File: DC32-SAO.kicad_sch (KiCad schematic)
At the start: 11 parts, among them J1 Conn_01x06_Male

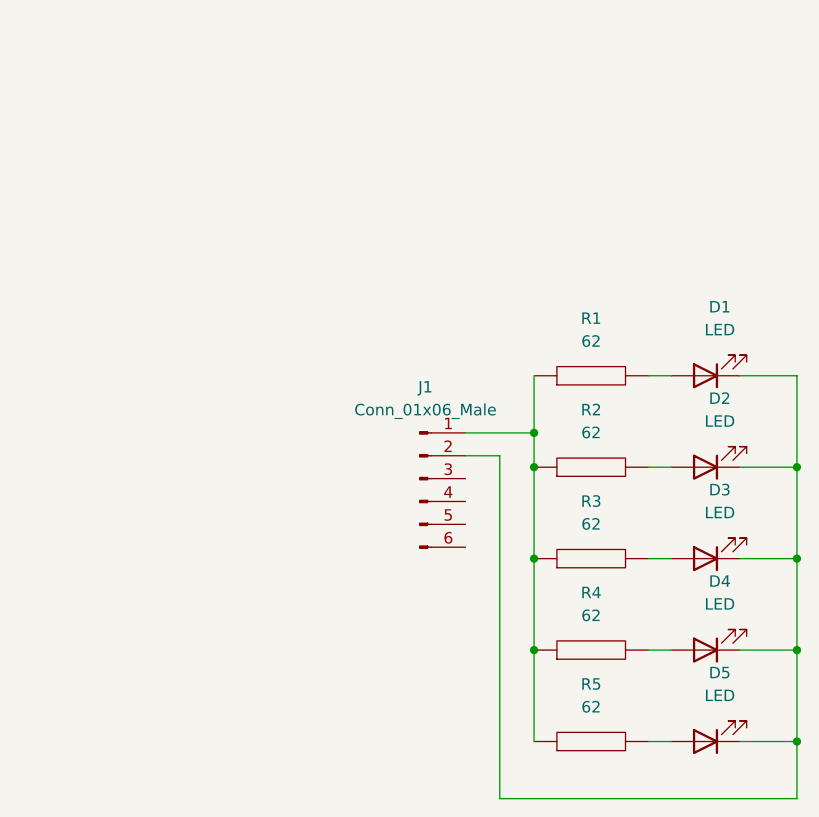
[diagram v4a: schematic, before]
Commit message: Changed Resistors to through-hole.
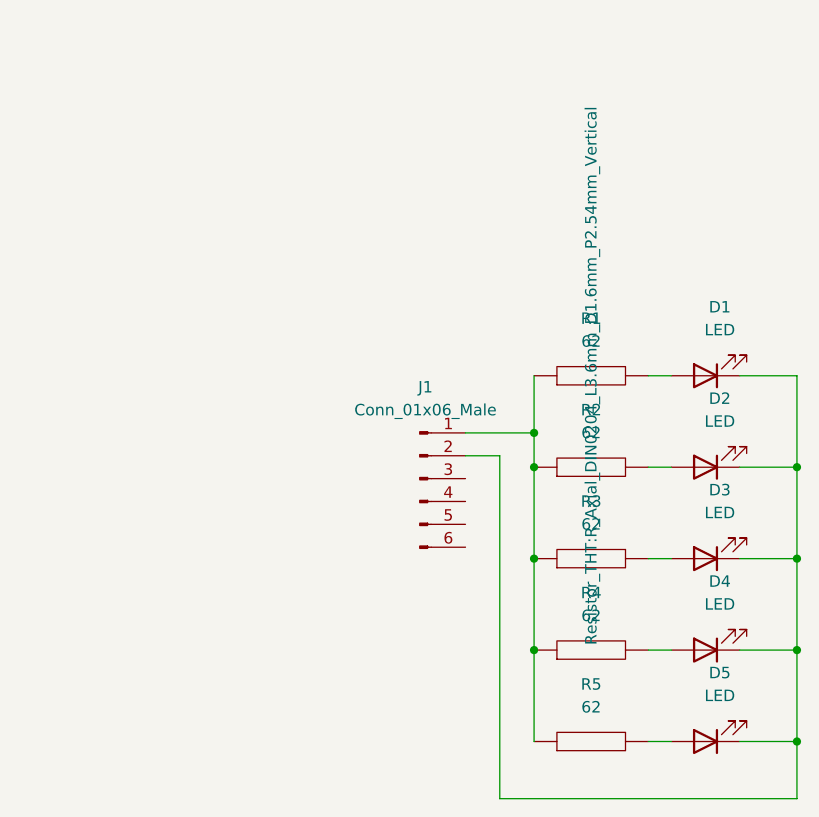
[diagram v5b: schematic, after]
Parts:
- R1, R2, R3, R4, R5: footprint Resistor_SMD:R_0603_1608Metric -> Resistor_THT:R_Axial_DIN0204_L3.6mm_D1.6mm_P2.54mm_Vertical
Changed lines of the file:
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@@
     (property "Reference" "R5" (id 0) (at 91.44 81.28 90))
     (property "Value" "62" (id 1) (at 91.44 83.82 90))
-    (property "Footprint" "Resistor_SMD:R_0603_1608Metric" (id 2) (at 91.44 87.63 0)
+    (property "Footprint" "Resistor_THT:R_Axial_DIN0204_L3.6mm_D1.6mm_P2.54mm_Vertical" (id 2) (at 91.44 87.63 0)
       (effects (font (size 1.27 1.27)) hide)
     )
@@
     (property "Reference" "R1" (id 0) (at 91.44 40.64 90))
     (property "Value" "62" (id 1) (at 91.44 43.18 90))
-    (property "Footprint" "Resistor_SMD:R_0603_1608Metric" (id 2) (at 91.44 46.99 0)
-      (effects (font (size 1.27 1.27)) hide)
-    )
+    (property "Footprint" "Resistor_THT:R_Axial_DIN0204_L3.6mm_D1.6mm_P2.54mm_Vertical" (id 2) (at 91.44 46.99 0))
     (property "Datasheet" "~" (id 3) (at 91.44 46.99 0)
       (effects (font (size 1.27 1.27)) hide)
@@
     (property "Reference" "R3" (id 0) (at 91.44 60.96 90))
     (property "Value" "62" (id 1) (at 91.44 63.5 90))
-    (property "Footprint" "Resistor_SMD:R_0603_1608Metric" (id 2) (at 91.44 67.31 0)
+    (property "Footprint" "Resistor_THT:R_Axial_DIN0204_L3.6mm_D1.6mm_P2.54mm_Vertical" (id 2) (at 91.44 67.31 0)
       (effects (font (size 1.27 1.27)) hide)
     )
@@
     (property "Reference" "R4" (id 0) (at 91.44 71.12 90))
     (property "Value" "62" (id 1) (at 91.44 73.66 90))
-    (property "Footprint" "Resistor_SMD:R_0603_1608Metric" (id 2) (at 91.44 77.47 0)
+    (property "Footprint" "Resistor_THT:R_Axial_DIN0204_L3.6mm_D1.6mm_P2.54mm_Vertical" (id 2) (at 91.44 77.47 0)
       (effects (font (size 1.27 1.27)) hide)
     )
@@
     (property "Reference" "R2" (id 0) (at 91.44 50.8 90))
     (property "Value" "62" (id 1) (at 91.44 53.34 90))
-    (property "Footprint" "Resistor_SMD:R_0603_1608Metric" (id 2) (at 91.44 57.15 0)
+    (property "Footprint" "Resistor_THT:R_Axial_DIN0204_L3.6mm_D1.6mm_P2.54mm_Vertical" (id 2) (at 91.44 57.15 0)
       (effects (font (size 1.27 1.27)) hide)
     )
@@
     )
     (path "/3224a758-6c5e-466b-a995-832667ce7042"
-      (reference "R1") (unit 1) (value "62") (footprint "Resistor_SMD:R_0603_1608Metric")
+      (reference "R1") (unit 1) (value "62") (footprint "Resistor_THT:R_Axial_DIN0204_L3.6mm_D1.6mm_P2.54mm_Vertical")
     )
     (path "/e52018b4-0166-44c3-88cb-627e4c30fa0d"
-      (reference "R2") (unit 1) (value "62") (footprint "Resistor_SMD:R_0603_1608Metric")
+      (reference "R2") (unit 1) (value "62") (footprint "Resistor_THT:R_Axial_DIN0204_L3.6mm_D1.6mm_P2.54mm_Vertical")
     )
     (path "/8fae0e04-1839-4e2c-8d18-18ef127a06b2"
-      (reference "R3") (unit 1) (value "62") (footprint "Resistor_SMD:R_0603_1608Metric")
+      (reference "R3") (unit 1) (value "62") (footprint "Resistor_THT:R_Axial_DIN0204_L3.6mm_D1.6mm_P2.54mm_Vertical")
     )
     (path "/d6cef32c-fe73-4c94-b806-d19f76d5f19f"
-      (reference "R4") (unit 1) (value "62") (footprint "Resistor_SMD:R_0603_1608Metric")
+      (reference "R4") (unit 1) (value "62") (footprint "Resistor_THT:R_Axial_DIN0204_L3.6mm_D1.6mm_P2.54mm_Vertical")
     )
     (path "/0c8e1220-c447-4528-8dc0-9ae09eaa4b36"
-      (reference "R5") (unit 1) (value "62") (footprint "Resistor_SMD:R_0603_1608Metric")
+      (reference "R5") (unit 1) (value "62") (footprint "Resistor_THT:R_Axial_DIN0204_L3.6mm_D1.6mm_P2.54mm_Vertical")
     )
   )

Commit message: Made through-hole version.
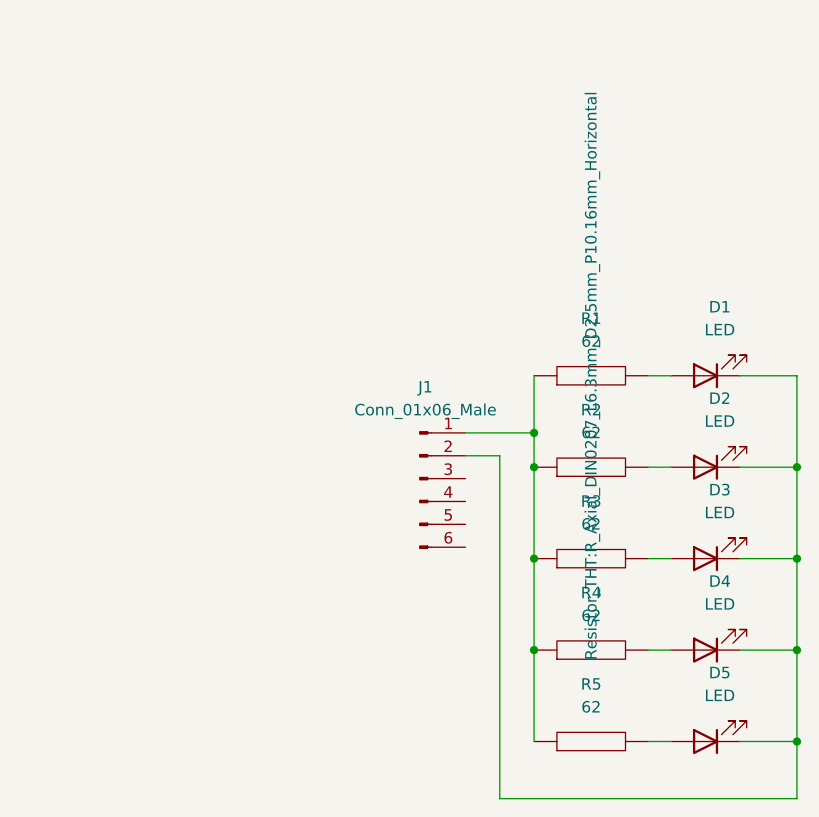
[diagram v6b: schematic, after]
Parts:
- J1: footprint Connector_PinHeader_2.54mm:PinHeader_2x03_P2.54mm_Vertical_SMD -> Connector_PinHeader_2.54mm:PinHeader_2x03_P2.54mm_Vertical
- R1, R2, R3, R4, R5: footprint Resistor_THT:R_Axial_DIN0204_L3.6mm_D1.6mm_P2.54mm_Vertical -> Resistor_THT:R_Axial_DIN0207_L6.3mm_D2.5mm_P10.16mm_Horizontal
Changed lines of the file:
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@@
     (property "Reference" "R5" (id 0) (at 91.44 81.28 90))
     (property "Value" "62" (id 1) (at 91.44 83.82 90))
-    (property "Footprint" "Resistor_THT:R_Axial_DIN0204_L3.6mm_D1.6mm_P2.54mm_Vertical" (id 2) (at 91.44 87.63 0)
+    (property "Footprint" "Resistor_THT:R_Axial_DIN0207_L6.3mm_D2.5mm_P10.16mm_Horizontal" (id 2) (at 91.44 87.63 0)
       (effects (font (size 1.27 1.27)) hide)
     )
@@
     (property "Reference" "R1" (id 0) (at 91.44 40.64 90))
     (property "Value" "62" (id 1) (at 91.44 43.18 90))
-    (property "Footprint" "Resistor_THT:R_Axial_DIN0204_L3.6mm_D1.6mm_P2.54mm_Vertical" (id 2) (at 91.44 46.99 0))
+    (property "Footprint" "Resistor_THT:R_Axial_DIN0207_L6.3mm_D2.5mm_P10.16mm_Horizontal" (id 2) (at 91.44 46.99 0))
     (property "Datasheet" "~" (id 3) (at 91.44 46.99 0)
       (effects (font (size 1.27 1.27)) hide)
@@
     (property "Reference" "J1" (id 0) (at 73.025 48.26 0))
     (property "Value" "Conn_01x06_Male" (id 1) (at 73.025 50.8 0))
-    (property "Footprint" "Connector_PinHeader_2.54mm:PinHeader_2x03_P2.54mm_Vertical_SMD" (id 2) (at 72.39 58.42 0)
+    (property "Footprint" "Connector_PinHeader_2.54mm:PinHeader_2x03_P2.54mm_Vertical" (id 2) (at 72.39 58.42 0)
       (effects (font (size 1.27 1.27)) hide)
     )
@@
     (property "Reference" "R3" (id 0) (at 91.44 60.96 90))
     (property "Value" "62" (id 1) (at 91.44 63.5 90))
-    (property "Footprint" "Resistor_THT:R_Axial_DIN0204_L3.6mm_D1.6mm_P2.54mm_Vertical" (id 2) (at 91.44 67.31 0)
+    (property "Footprint" "Resistor_THT:R_Axial_DIN0207_L6.3mm_D2.5mm_P10.16mm_Horizontal" (id 2) (at 91.44 67.31 0)
       (effects (font (size 1.27 1.27)) hide)
     )
@@
     (property "Reference" "R4" (id 0) (at 91.44 71.12 90))
     (property "Value" "62" (id 1) (at 91.44 73.66 90))
-    (property "Footprint" "Resistor_THT:R_Axial_DIN0204_L3.6mm_D1.6mm_P2.54mm_Vertical" (id 2) (at 91.44 77.47 0)
+    (property "Footprint" "Resistor_THT:R_Axial_DIN0207_L6.3mm_D2.5mm_P10.16mm_Horizontal" (id 2) (at 91.44 77.47 0)
       (effects (font (size 1.27 1.27)) hide)
     )
@@
     (property "Reference" "R2" (id 0) (at 91.44 50.8 90))
     (property "Value" "62" (id 1) (at 91.44 53.34 90))
-    (property "Footprint" "Resistor_THT:R_Axial_DIN0204_L3.6mm_D1.6mm_P2.54mm_Vertical" (id 2) (at 91.44 57.15 0)
+    (property "Footprint" "Resistor_THT:R_Axial_DIN0207_L6.3mm_D2.5mm_P10.16mm_Horizontal" (id 2) (at 91.44 57.15 0)
       (effects (font (size 1.27 1.27)) hide)
     )
@@
     )
     (path "/5681b4fd-442e-49d7-8fe1-5d17e8cfa0a0"
-      (reference "J1") (unit 1) (value "Conn_01x06_Male") (footprint "Connector_PinHeader_2.54mm:PinHeader_2x03_P2.54mm_Vertical_SMD")
+      (reference "J1") (unit 1) (value "Conn_01x06_Male") (footprint "Connector_PinHeader_2.54mm:PinHeader_2x03_P2.54mm_Vertical")
     )
     (path "/3224a758-6c5e-466b-a995-832667ce7042"
-      (reference "R1") (unit 1) (value "62") (footprint "Resistor_THT:R_Axial_DIN0204_L3.6mm_D1.6mm_P2.54mm_Vertical")
+      (reference "R1") (unit 1) (value "62") (footprint "Resistor_THT:R_Axial_DIN0207_L6.3mm_D2.5mm_P10.16mm_Horizontal")
     )
     (path "/e52018b4-0166-44c3-88cb-627e4c30fa0d"
-      (reference "R2") (unit 1) (value "62") (footprint "Resistor_THT:R_Axial_DIN0204_L3.6mm_D1.6mm_P2.54mm_Vertical")
+      (reference "R2") (unit 1) (value "62") (footprint "Resistor_THT:R_Axial_DIN0207_L6.3mm_D2.5mm_P10.16mm_Horizontal")
     )
     (path "/8fae0e04-1839-4e2c-8d18-18ef127a06b2"
-      (reference "R3") (unit 1) (value "62") (footprint "Resistor_THT:R_Axial_DIN0204_L3.6mm_D1.6mm_P2.54mm_Vertical")
+      (reference "R3") (unit 1) (value "62") (footprint "Resistor_THT:R_Axial_DIN0207_L6.3mm_D2.5mm_P10.16mm_Horizontal")
     )
     (path "/d6cef32c-fe73-4c94-b806-d19f76d5f19f"
-      (reference "R4") (unit 1) (value "62") (footprint "Resistor_THT:R_Axial_DIN0204_L3.6mm_D1.6mm_P2.54mm_Vertical")
+      (reference "R4") (unit 1) (value "62") (footprint "Resistor_THT:R_Axial_DIN0207_L6.3mm_D2.5mm_P10.16mm_Horizontal")
     )
     (path "/0c8e1220-c447-4528-8dc0-9ae09eaa4b36"
-      (reference "R5") (unit 1) (value "62") (footprint "Resistor_THT:R_Axial_DIN0204_L3.6mm_D1.6mm_P2.54mm_Vertical")
+      (reference "R5") (unit 1) (value "62") (footprint "Resistor_THT:R_Axial_DIN0207_L6.3mm_D2.5mm_P10.16mm_Horizontal")
     )
   )

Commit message: Updates.
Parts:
- removed J1: Conn_01x06_Male, Connector_PinHeader_2.54mm:PinHeader_2x03_P2.54mm_Vertical, symbol Connector:Conn_01x06_Male
- added J1: Conn_01x02_Male, Battery:BatteryHolder_Keystone_3002_1x2032, symbol Connector:Conn_01x02_Male
- added SW1: SW_Push_DPDT, Button_Switch_THT:SW_CuK_JS202011CQN_DPDT_Straight, symbol Switch:SW_Push_DPDT
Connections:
- net at D1.1 (K), D2.1 (K), D3.1 (K)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: now also J1.2 (Pin_2)
- net at R1.1, R2.1, R3.1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: now also SW1.1 (A)
- new net: J1.1 (Pin_1), SW1.2 (B)
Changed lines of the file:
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@@
     (stroke (width 0) (type default) (color 0 0 0 0))
   )
-  (wire (pts (xy 77.47 53.34) (xy 85.09 53.34))
+  (wire (pts (xy 63.5 53.34) (xy 85.09 53.34))
+    (stroke (width 0) (type default) (color 0 0 0 0))
+  )
+  (wire (pts (xy 41.91 58.42) (xy 41.91 93.98))
     (stroke (width 0) (type default) (color 0 0 0 0))
   )
@@
     (stroke (width 0) (type default) (color 0 0 0 0))
   )
-  (wire (pts (xy 77.47 55.88) (xy 81.28 55.88))
-    (stroke (width 0) (type default) (color 0 0 0 0))
-  )
   (wire (pts (xy 97.79 67.31) (xy 100.33 67.31))
     (stroke (width 0) (type default) (color 0 0 0 0))
   )
-  (wire (pts (xy 114.3 93.98) (xy 81.28 93.98))
+  (wire (pts (xy 41.91 93.98) (xy 114.3 93.98))
+    (stroke (width 0) (type default) (color 0 0 0 0))
+  )
+  (wire (pts (xy 41.91 55.88) (xy 53.34 55.88))
     (stroke (width 0) (type default) (color 0 0 0 0))
   )
@@
   )
   (wire (pts (xy 85.09 67.31) (xy 85.09 77.47))
-    (stroke (width 0) (type default) (color 0 0 0 0))
-  )
-  (wire (pts (xy 81.28 55.88) (xy 81.28 93.98))
     (stroke (width 0) (type default) (color 0 0 0 0))
   )
@@
     (pin "2")
   )
-  (symbol (lib_id "Connector:Conn_01x06_Male") (at 72.39 58.42 0) (unit 1)
-    (in_bom yes) (on_board yes) (fields_autoplaced)
-    (property "Reference" "J1" (id 0) (at 73.025 48.26 0))
-    (property "Value" "Conn_01x06_Male" (id 1) (at 73.025 50.8 0))
-    (property "Footprint" "Connector_PinHeader_2.54mm:PinHeader_2x03_P2.54mm_Vertical" (id 2) (at 72.39 58.42 0)
-      (effects (font (size 1.27 1.27)) hide)
-    )
-    (property "Datasheet" "~" (id 3) (at 72.39 58.42 0)
+  (symbol (lib_id "pspice:R") (at 91.44 67.31 90) (unit 1)
+    (in_bom yes) (on_board yes) (fields_autoplaced)
+    (property "Reference" "R3" (id 0) (at 91.44 60.96 90))
+    (property "Value" "62" (id 1) (at 91.44 63.5 90))
+    (property "Footprint" "Resistor_THT:R_Axial_DIN0207_L6.3mm_D2.5mm_P10.16mm_Horizontal" (id 2) (at 91.44 67.31 0)
+      (effects (font (size 1.27 1.27)) hide)
+    )
+    (property "Datasheet" "~" (id 3) (at 91.44 67.31 0)
+      (effects (font (size 1.27 1.27)) hide)
+    )
+    (pin "1")
+    (pin "2")
+  )
+  (symbol (lib_id "Connector:Conn_01x02_Male") (at 36.83 55.88 0) (unit 1)
+    (in_bom yes) (on_board yes) (fields_autoplaced)
+    (property "Reference" "J1" (id 0) (at 37.465 50.8 0))
+    (property "Value" "Conn_01x02_Male" (id 1) (at 37.465 53.34 0))
+    (property "Footprint" "Battery:BatteryHolder_Keystone_3002_1x2032" (id 2) (at 36.83 55.88 0)
+      (effects (font (size 1.27 1.27)) hide)
+    )
+    (property "Datasheet" "~" (id 3) (at 36.83 55.88 0)
+      (effects (font (size 1.27 1.27)) hide)
+    )
+    (pin "1")
+    (pin "2")
+  )
+  (symbol (lib_id "Device:LED") (at 104.14 87.63 180) (unit 1)
+    (in_bom yes) (on_board yes) (fields_autoplaced)
+    (property "Reference" "D5" (id 0) (at 105.7275 80.01 0))
+    (property "Value" "LED" (id 1) (at 105.7275 82.55 0))
+    (property "Footprint" "LED_THT:LED_D3.0mm" (id 2) (at 104.14 87.63 0)
+      (effects (font (size 1.27 1.27)) hide)
+    )
+    (property "Datasheet" "~" (id 3) (at 104.14 87.63 0)
+      (effects (font (size 1.27 1.27)) hide)
+    )
+    (pin "1")
+    (pin "2")
+  )
+  (symbol (lib_id "Switch:SW_Push_DPDT") (at 58.42 60.96 0) (unit 1)
+    (in_bom yes) (on_board yes) (fields_autoplaced)
+    (property "Reference" "SW1" (id 0) (at 58.42 48.26 0))
+    (property "Value" "SW_Push_DPDT" (id 1) (at 58.42 50.8 0))
+    (property "Footprint" "Button_Switch_THT:SW_CuK_JS202011CQN_DPDT_Straight" (id 2) (at 58.42 55.88 0)
+      (effects (font (size 1.27 1.27)) hide)
+    )
+    (property "Datasheet" "~" (id 3) (at 58.42 55.88 0)
       (effects (font (size 1.27 1.27)) hide)
     )
@@
     (pin "6")
   )
-  (symbol (lib_id "pspice:R") (at 91.44 67.31 90) (unit 1)
-    (in_bom yes) (on_board yes) (fields_autoplaced)
-    (property "Reference" "R3" (id 0) (at 91.44 60.96 90))
-    (property "Value" "62" (id 1) (at 91.44 63.5 90))
-    (property "Footprint" "Resistor_THT:R_Axial_DIN0207_L6.3mm_D2.5mm_P10.16mm_Horizontal" (id 2) (at 91.44 67.31 0)
-      (effects (font (size 1.27 1.27)) hide)
-    )
-    (property "Datasheet" "~" (id 3) (at 91.44 67.31 0)
-      (effects (font (size 1.27 1.27)) hide)
-    )
-    (pin "1")
-    (pin "2")
-  )
-  (symbol (lib_id "Device:LED") (at 104.14 87.63 180) (unit 1)
-    (in_bom yes) (on_board yes) (fields_autoplaced)
-    (property "Reference" "D5" (id 0) (at 105.7275 80.01 0))
-    (property "Value" "LED" (id 1) (at 105.7275 82.55 0))
-    (property "Footprint" "LED_THT:LED_D3.0mm" (id 2) (at 104.14 87.63 0)
-      (effects (font (size 1.27 1.27)) hide)
-    )
-    (property "Datasheet" "~" (id 3) (at 104.14 87.63 0)
-      (effects (font (size 1.27 1.27)) hide)
-    )
-    (pin "1")
-    (pin "2")
-  )
   (symbol (lib_id "pspice:R") (at 91.44 77.47 90) (unit 1)
     (in_bom yes) (on_board yes) (fields_autoplaced)
@@
       (reference "D5") (unit 1) (value "LED") (footprint "LED_THT:LED_D3.0mm")
     )
-    (path "/5681b4fd-442e-49d7-8fe1-5d17e8cfa0a0"
-      (reference "J1") (unit 1) (value "Conn_01x06_Male") (footprint "Connector_PinHeader_2.54mm:PinHeader_2x03_P2.54mm_Vertical")
+    (path "/9083bc61-5ef0-4c4f-b6fe-0b8c6ffc3688"
+      (reference "J1") (unit 1) (value "Conn_01x02_Male") (footprint "Battery:BatteryHolder_Keystone_3002_1x2032")
     )
     (path "/3224a758-6c5e-466b-a995-832667ce7042"
@@
       (reference "R5") (unit 1) (value "62") (footprint "Resistor_THT:R_Axial_DIN0207_L6.3mm_D2.5mm_P10.16mm_Horizontal")
     )
-  )
+    (path "/b8fa9f31-01c4-4c21-95ef-07462a8824ca"
+      (reference "SW1") (unit 1) (value "SW_Push_DPDT") (footprint "Button_Switch_THT:SW_CuK_JS202011CQN_DPDT_Straight")
+    )
+  )
